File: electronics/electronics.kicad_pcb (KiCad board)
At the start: 2 copper layers, 58 x 58 mm, 5 parts, among them U1 ESP32-C6-WROOM-1

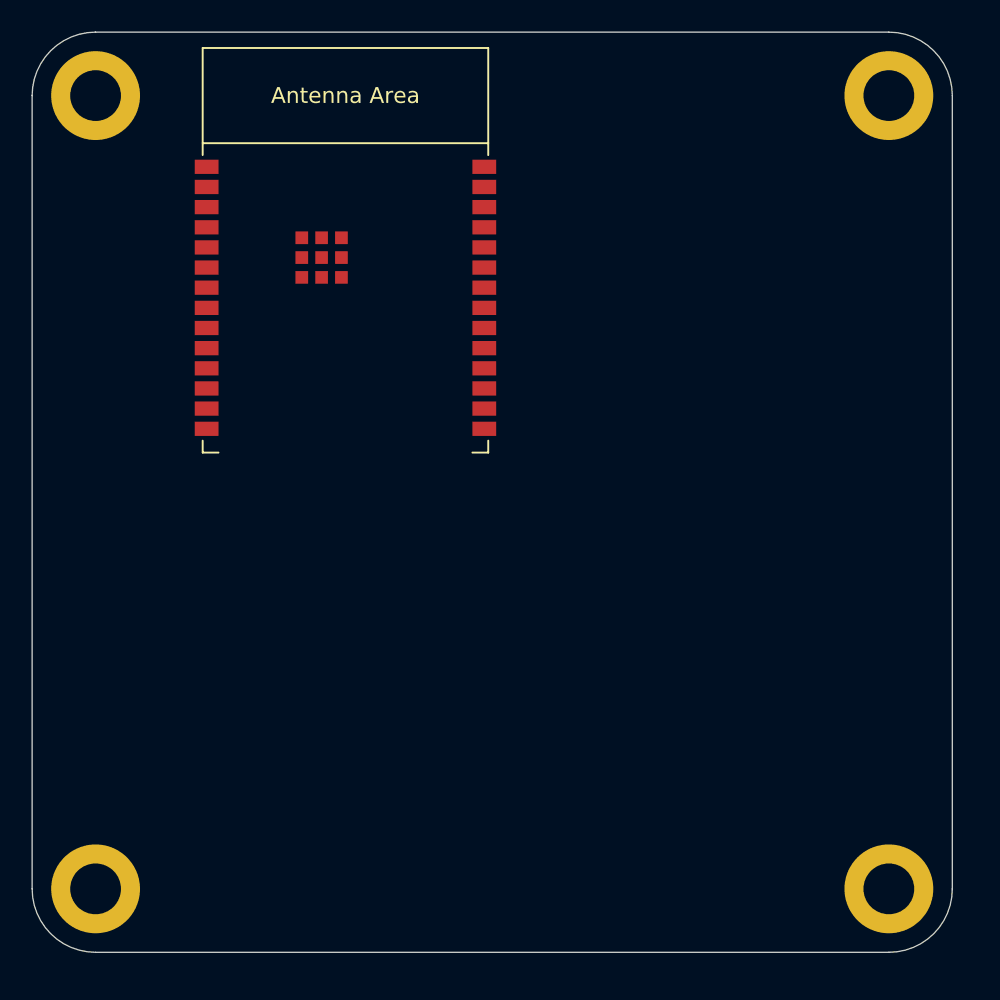
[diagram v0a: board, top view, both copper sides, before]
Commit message: hardware: add pcb cutouts
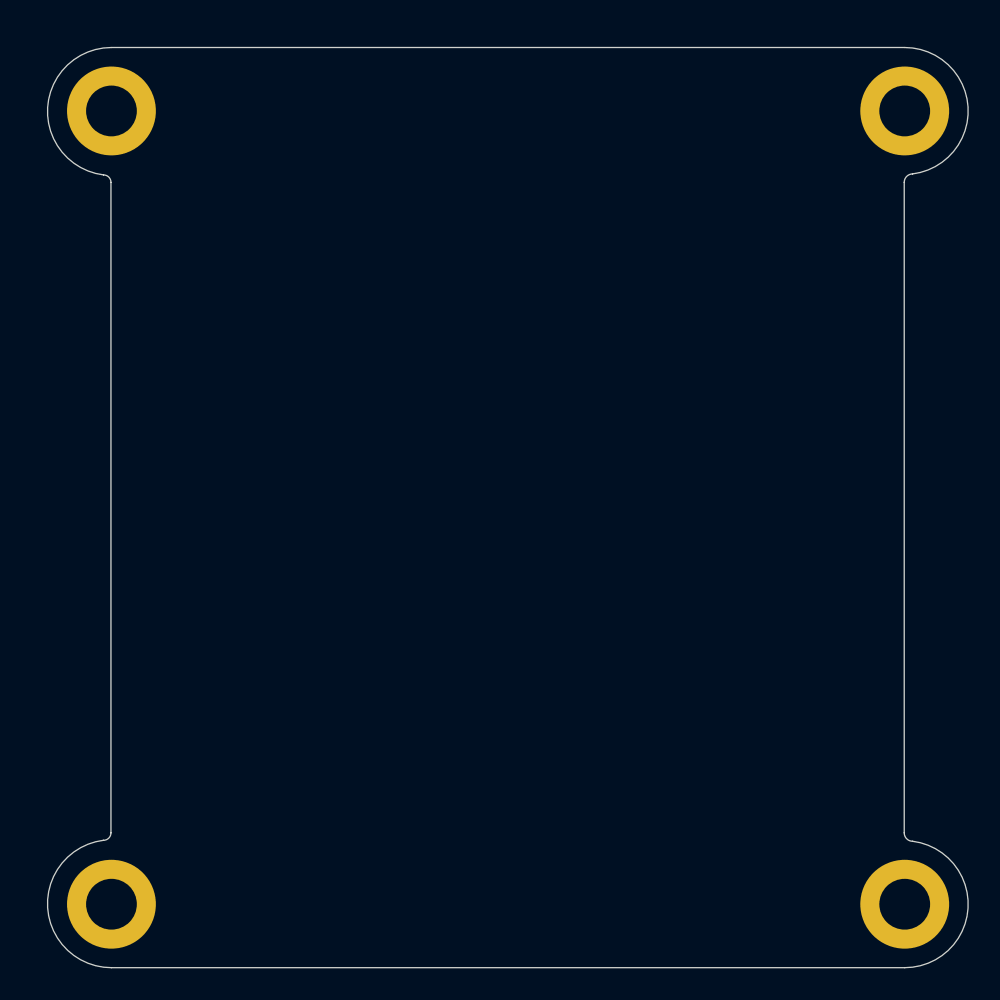
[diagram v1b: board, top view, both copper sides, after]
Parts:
- removed U1: ESP32-C6-WROOM-1, PCM_Espressif:ESP32-C6-WROOM-1
- moved H1 1.39 mm to (25.0, 25.0)
- moved H2 1.39 mm to (75.0, 25.0)
- moved H3 1.39 mm to (25.0, 75.0)
- moved H4 1.39 mm to (75.0, 75.0)
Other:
- outline, holes or cut-outs redrawn

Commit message: pcb: add mcu, power regulator and usb-c connector
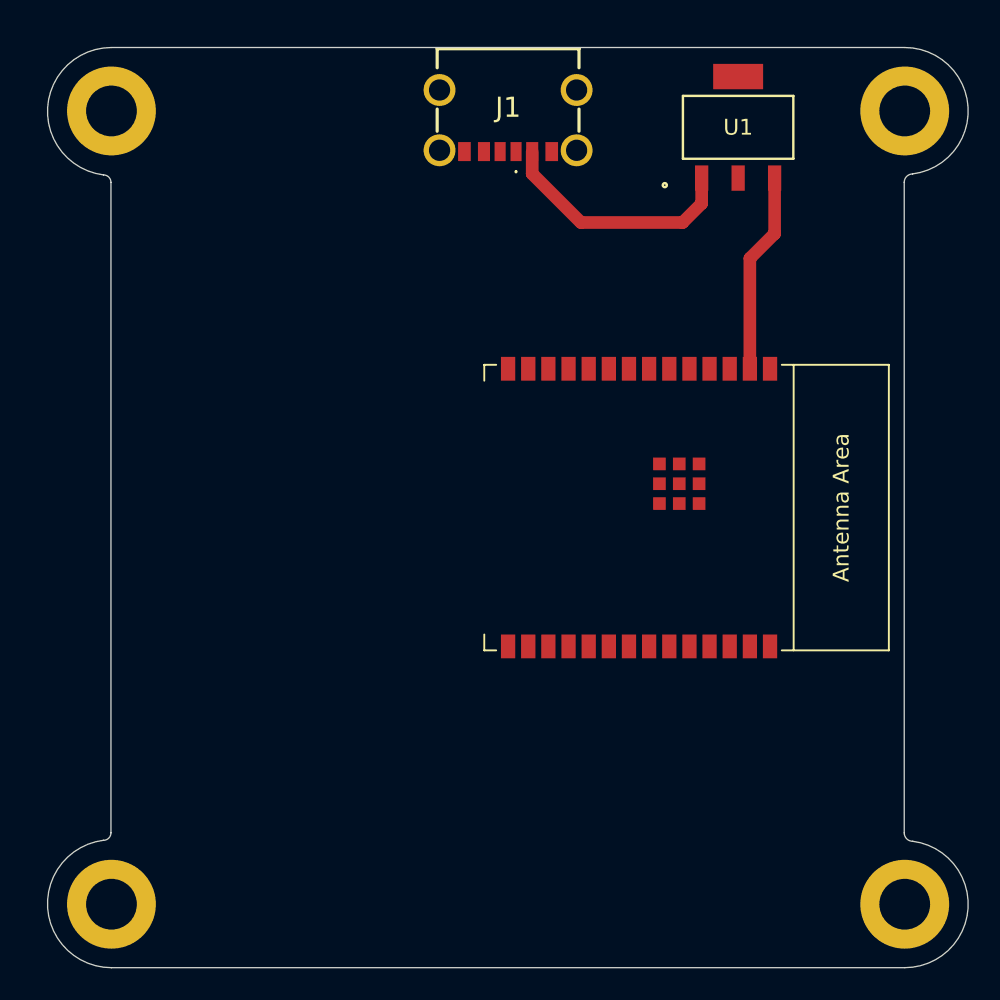
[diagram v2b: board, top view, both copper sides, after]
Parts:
- added J1: USB4125-GF-A, footprints:USB4125GFA, F.Cu at (50.0, 24.8)
- added U1: LM3940IMP-3.3, footprints:MP04A, F.Cu at (64.5, 26.0)
- added U2: ESP32-C6-WROOM-1, PCM_Espressif:ESP32-C6-WROOM-1, F.Cu at (58.2, 50.0)
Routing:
- net +5V: track 0.00 -> 15.4 mm
- net +3V3: track 0.00 -> 12.7 mm

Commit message: pcb: add usb power and data connections
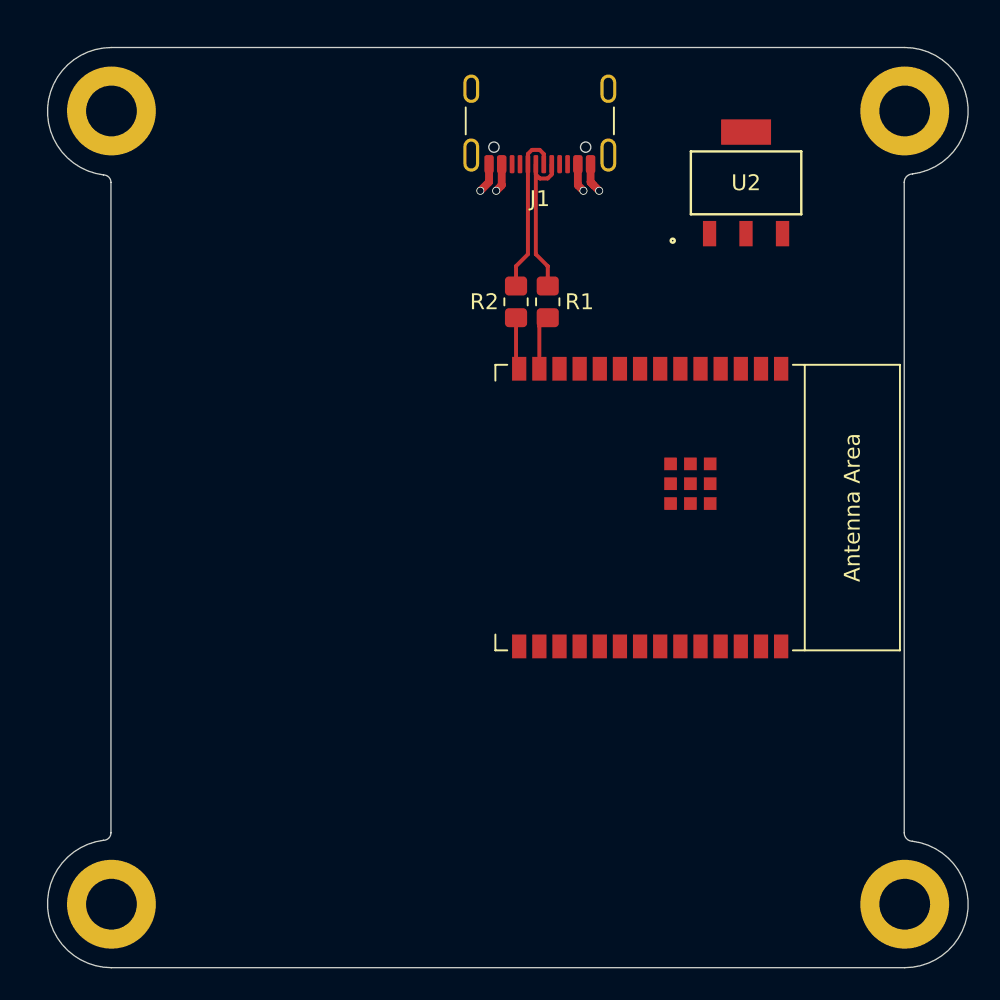
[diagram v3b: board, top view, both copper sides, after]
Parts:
- added R1: 22R, Resistor_SMD:R_0805_2012Metric_Pad1.20x1.40mm_HandSolder, F.Cu at (52.5, 37.0)
- added R2: 22R, Resistor_SMD:R_0805_2012Metric_Pad1.20x1.40mm_HandSolder, F.Cu at (50.5, 37.0)
- J1: value USB4125-GF-A -> USB_C_Receptacle_USB2.0_16P; footprint footprints:USB4125GFA -> Connector_USB:USB_C_Receptacle_GCT_USB4105-xx-A_16P_TopMnt_Horizontal
- U1: value LM3940IMP-3.3 -> ESP32-C6-WROOM-1; footprint footprints:MP04A -> PCM_Espressif:ESP32-C6-WROOM-1
- U2: value ESP32-C6-WROOM-1 -> LM3940IMP-3.3; footprint PCM_Espressif:ESP32-C6-WROOM-1 -> footprints:MP04A
- moved U1 24.6 mm to (59.0, 50.0), turned to -90 degrees
- moved U2 21.6 mm to (65.0, 29.5), turned to 0 degrees
- moved J1 2.00 mm to (52.0, 24.6)
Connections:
- J1 pad A12: unconnected-(J1-GND_1-PadA12) -> GND
- U1 pad 1: +5V -> GND
- U1 pad 2: GND -> +3V3
- U1 pad 3: +3V3 -> unconnected-(U1-EN/CHIP_PU-Pad3)
- U2 pad 1: GND -> +5V
- U2 pad 2: +3V3 -> GND
- U2 pad 3: unconnected-(U2-EN/CHIP_PU-Pad3) -> +3V3
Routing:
- net +3V3: track 12.7 -> 0.00 mm
- net +5V: track 15.4 -> 3.64 mm, vias 0 -> 2
- net Net-(J1-D--PadA7): track 0.00 -> 10.5 mm
- net Net-(J1-D+-PadA6): track 0.00 -> 10.5 mm
- net GND: track 0.00 -> 3.80 mm, vias 0 -> 2
- net USB_D-: track 0.00 -> 3.47 mm
- net USB_D+: track 0.00 -> 3.30 mm

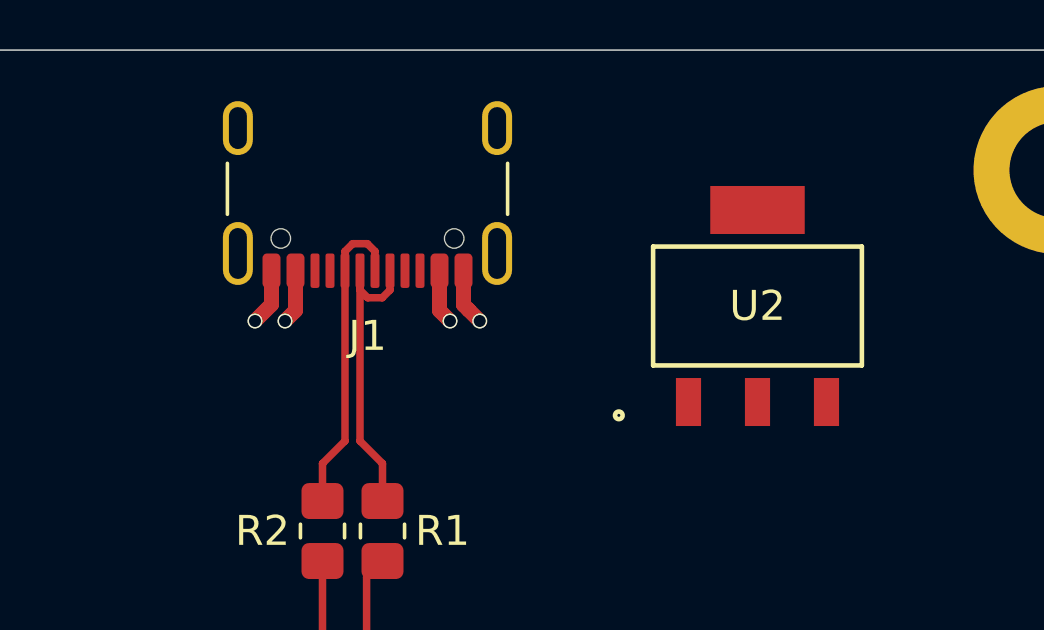
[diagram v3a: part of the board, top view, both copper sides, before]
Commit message: pcb: add 5.1k pull-downs to usb cc1/cc2 to pcb
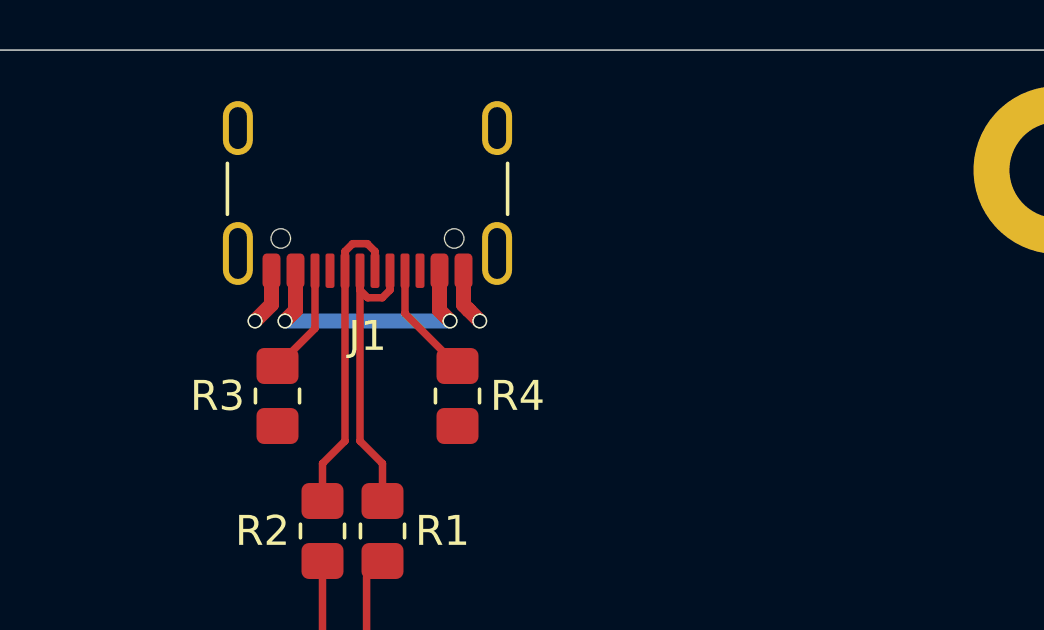
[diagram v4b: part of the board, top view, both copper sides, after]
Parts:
- removed U2: LM3940IMP-3.3, footprints:MP04A
- added R3: 5.1K, Resistor_SMD:R_0805_2012Metric_Pad1.20x1.40mm_HandSolder, F.Cu at (49.0, 32.5)
- added R4: 5.1K, Resistor_SMD:R_0805_2012Metric_Pad1.20x1.40mm_HandSolder, F.Cu at (55.0, 32.5)
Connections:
- J1 pad A5: unconnected-(J1-CC1-PadA5) -> Net-(J1-CC1)
- J1 pad B5: unconnected-(J1-CC2-PadB5) -> Net-(J1-CC2)
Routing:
- net +5V: track 3.64 -> 9.14 mm
- net Net-(J1-CC1): track 0.00 -> 3.90 mm
- net Net-(J1-CC2): track 0.00 -> 3.69 mm

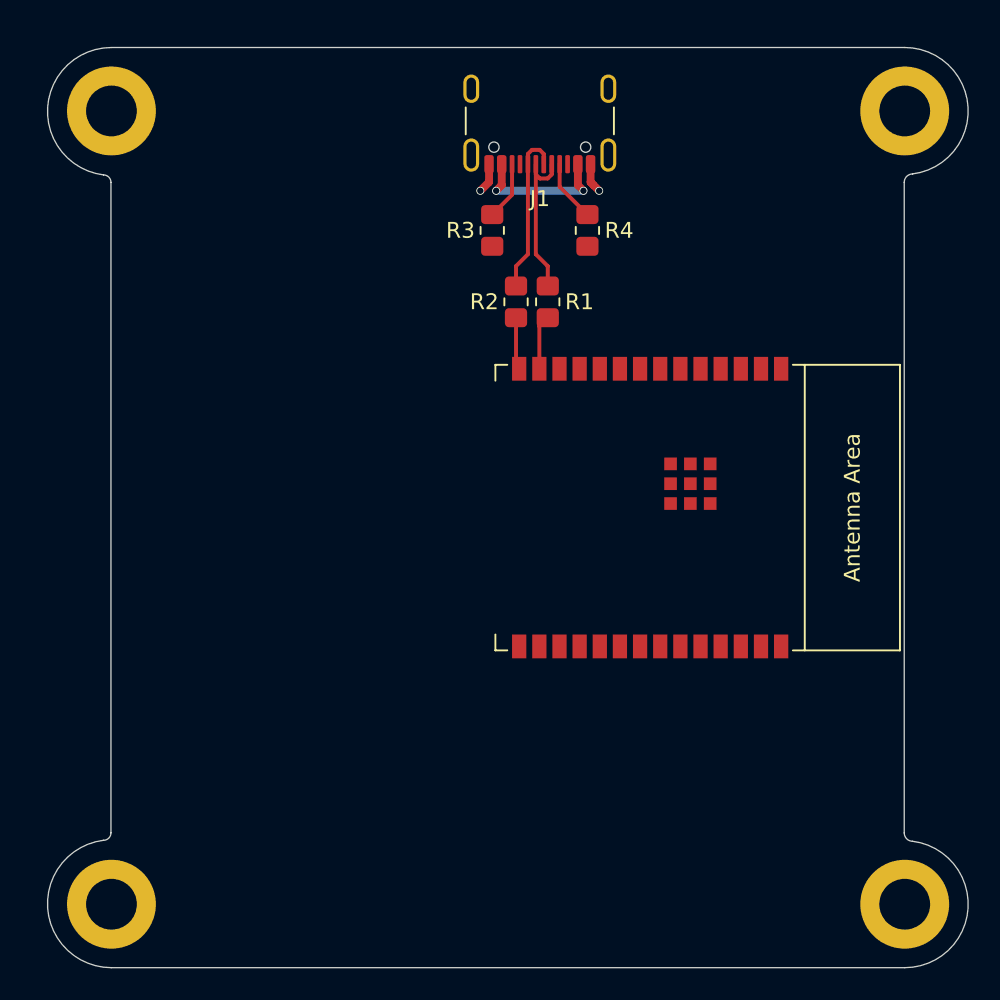
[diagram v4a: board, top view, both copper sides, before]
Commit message: pcb: add am2320
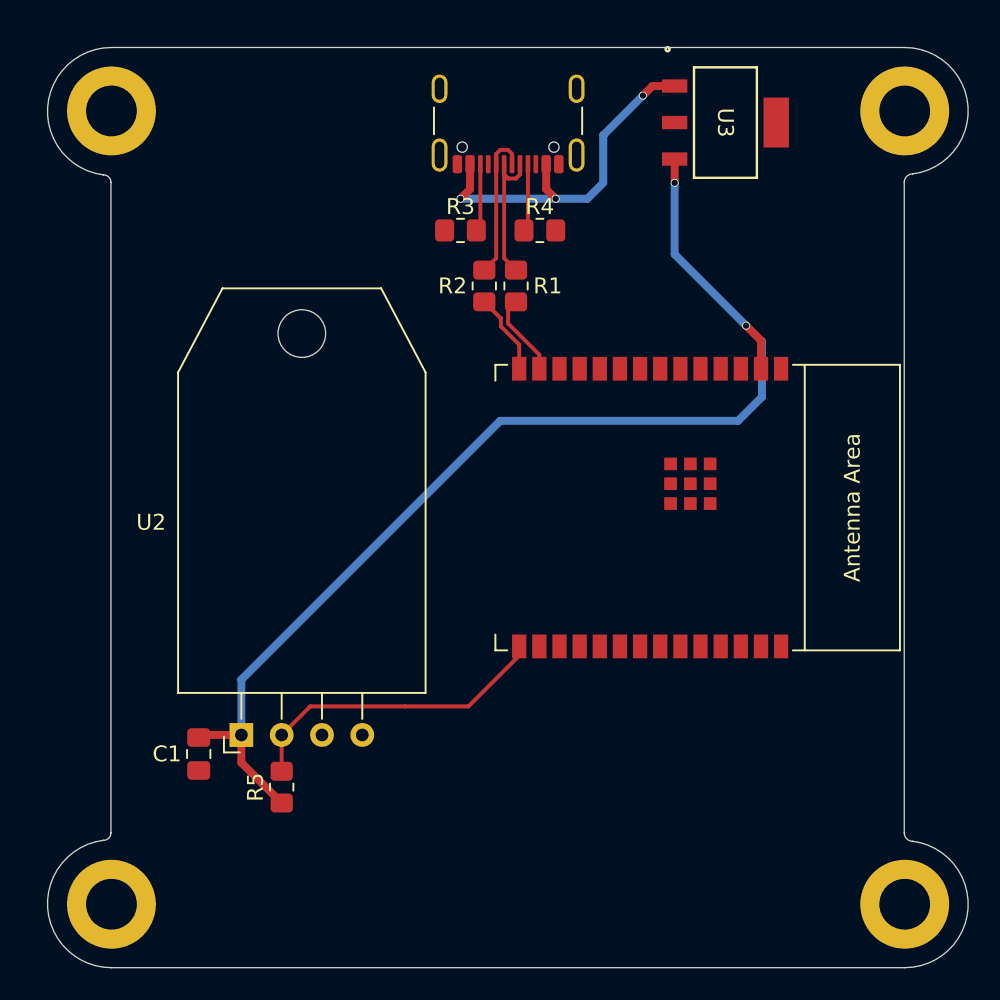
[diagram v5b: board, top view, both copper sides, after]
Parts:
- added C1: 100C, Capacitor_SMD:C_0805_2012Metric_Pad1.18x1.45mm_HandSolder, F.Cu at (30.5, 65.5)
- added R5: 4.7K, Resistor_SMD:R_0805_2012Metric_Pad1.20x1.40mm_HandSolder, F.Cu at (35.7, 67.6)
- added U2: AM2302, Sensor:ASAIR_AM2302_P2.54mm_Lead2.75mm_TabDown, F.Cu at (33.2, 64.3)
- added U3: LM3940IMP-3.3, footprints:MP04A, F.Cu at (63.7, 25.7)
- moved R4 3.00 mm to (52.0, 32.5), turned to 0 degrees
- moved R1 2.24 mm to (50.5, 36.0)
- moved R2 2.24 mm to (48.5, 36.0)
- moved J1 2.00 mm to (50.0, 24.6)
- moved R3 2.00 mm to (47.0, 32.5), turned to 180 degrees
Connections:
- U1 pad 15: unconnected-(U1-GPIO9-Pad15) -> AM2302_SDA
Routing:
- net +3V3: track 0.00 -> 72.2 mm, vias 0 -> 2
- net AM2302_SDA: track 0.00 -> 19.9 mm
- net +5V: track 9.14 -> 23.0 mm, vias 2 -> 3
- net GND: track 3.80 -> 0.00 mm, vias 2 -> 0
- net USB_D+: track 3.30 -> 5.13 mm
- net USB_D-: track 3.47 -> 5.24 mm
- net Net-(J1-D--PadA7): track 10.5 -> 9.49 mm
- net Net-(J1-D+-PadA6): track 10.5 -> 9.49 mm
- net Net-(J1-CC2): track 3.69 -> 4.28 mm
